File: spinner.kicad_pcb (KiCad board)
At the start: 2 copper layers, 190 x 190 mm, 87 parts, among them J1 Micro_SD_Card, SW1 SW_SPDT, U1 AP63205WU, U2 RS0102, U3 SFH617A-3X006, U4 SFH617A-3X006, U5 SFH617A-3X006

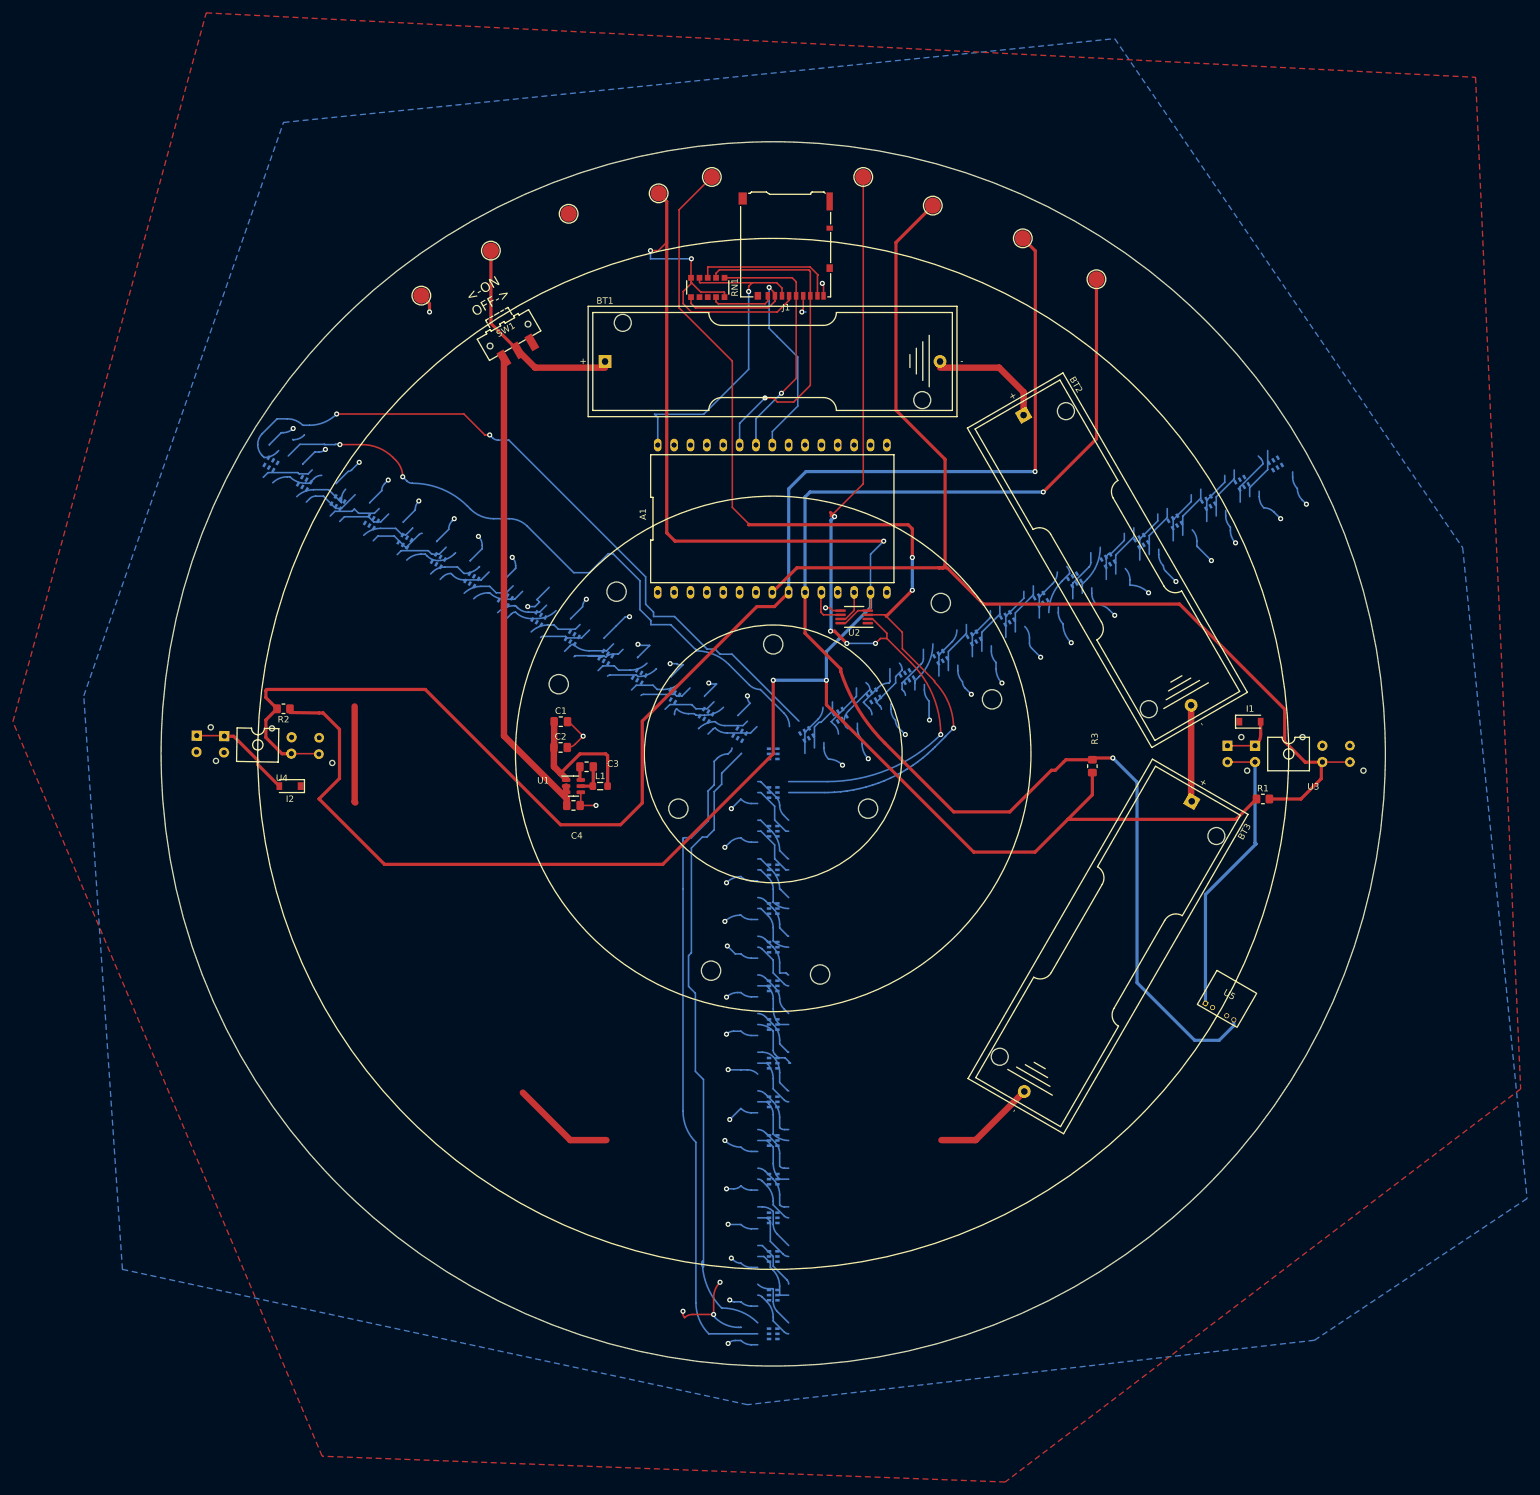
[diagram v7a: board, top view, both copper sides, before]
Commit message: Place little LEDs into 3 rows.
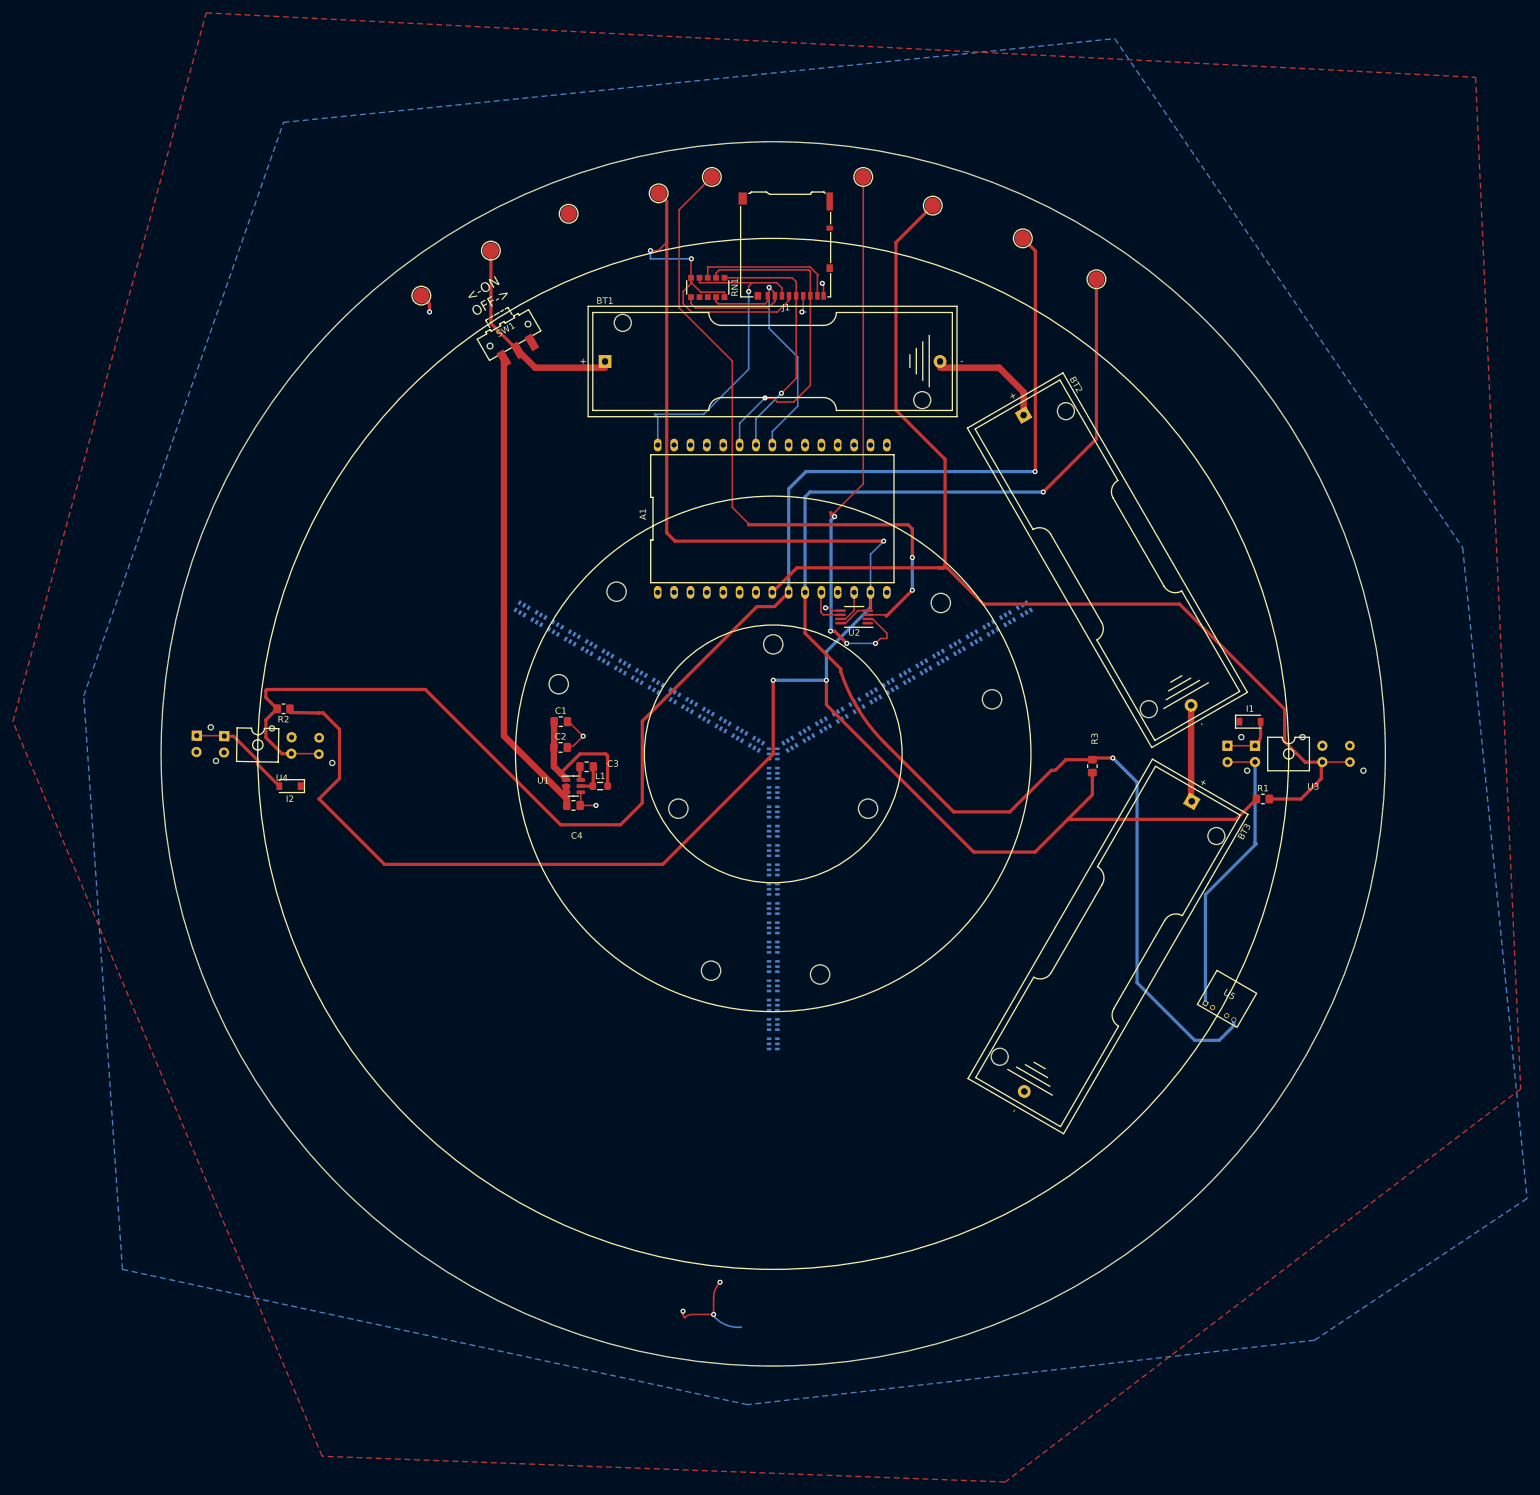
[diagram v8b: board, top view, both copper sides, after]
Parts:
- moved D115 45.0 mm to (150.0, 145.0), turned to 0 degrees
- moved D215 45.0 mm to (111.0, 77.5), turned to -120 degrees
- moved D315 45.0 mm to (189.0, 77.5), turned to 120 degrees
- moved D314 42.0 mm to (186.4, 79.0), turned to 120 degrees
- moved D214 42.0 mm to (113.6, 79.0), turned to -120 degrees
- moved D114 42.0 mm to (150.0, 142.0), turned to 0 degrees
- moved D113 39.0 mm to (150.0, 139.0), turned to 0 degrees
- moved D213 39.0 mm to (116.2, 80.5), turned to -120 degrees
- moved D313 39.0 mm to (183.8, 80.5), turned to 120 degrees
- moved D112 36.0 mm to (150.0, 136.0), turned to 0 degrees
- moved D212 36.0 mm to (118.8, 82.0), turned to -120 degrees
- moved D312 36.0 mm to (181.2, 82.0), turned to 120 degrees
- moved D311 33.0 mm to (178.6, 83.5), turned to 120 degrees
- moved D211 33.0 mm to (121.4, 83.5), turned to -120 degrees
- moved D111 33.0 mm to (150.0, 133.0), turned to 0 degrees
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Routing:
- net VCC: track 313.1 -> 23.0 mm, vias 45 -> 0
- net GND: track 203.5 -> 37.1 mm
- net Net-(D214-Pad5): track 122.8 -> 0.00 mm, vias 2 -> 0
- net /CO_1: track 113.0 -> 0.00 mm
- net /DO_3: track 110.2 -> 0.00 mm, vias 2 -> 0
- net /DO_1: track 107.8 -> 0.00 mm
- net /CI: track 163.0 -> 104.5 mm, vias 3 -> 2
- net /DI: track 132.0 -> 88.9 mm, vias 5 -> 4
- net (no net): track 39.7 -> 0.00 mm
- net Net-(D302-Pad6): track 27.4 -> 0.00 mm
- net Net-(D213-Pad6): track 26.9 -> 0.00 mm
- net Net-(D102-Pad5): track 25.1 -> 0.00 mm
- net Net-(D204-Pad6): track 19.3 -> 0.00 mm
- net Net-(D209-Pad5): track 18.1 -> 0.00 mm
- net Net-(D103-Pad5): track 17.6 -> 0.00 mm
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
